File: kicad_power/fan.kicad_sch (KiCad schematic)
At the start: 5 parts, among them M1 Fan, Q5 2N7002E, U7 SFH617A-1X007T

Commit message: finished initial layout of power stage in KiCAD
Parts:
- M1: now left out of the parts list
- Q5: Partno (none) -> 2N7002E-T1-GE3
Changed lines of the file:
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@@
 			)
 		)
-		(property "Description" "Resistor"
+		(property "Description" "125mW Thin Film Resistor ±25ppm/℃ ±0.1% 2kΩ 0603 Chip Resistor - Surface Mount ROHS"
 			(at 152.4 92.71 0)
 			(effects
@@
 		(unit 1)
 		(exclude_from_sim no)
-		(in_bom yes)
+		(in_bom no)
 		(on_board yes)
 		(dnp no)
@@
 			)
 		)
-		(property "Description" "Resistor"
+		(property "Description" "Res Thick Film 0603 430 Ohm 1% 0.25W(1/4W) ±100ppm/C Pad SMD T/R Automotive AEC-Q200"
 			(at 118.11 101.6 0)
 			(effects
@@
 			(at 165.1 85.09 0)
 			(effects
+				(font
+					(size 1.27 1.27)
+				)
+				(hide yes)
+			)
+		)
+		(property "Partno" "2N7002E-T1-GE3"
+			(at 165.1 85.09 0)
+			(effects
+				(font
+					(size 1.27 1.27)
+				)
+				(hide yes)
+			)
+		)
+		(property "Field6" ""
+			(at 165.1 85.09 0)
+			(effects

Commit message: adjustment to PCB layout, created BOM file, added MOSFET gate discharge diodes
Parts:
- M1: now in the parts list
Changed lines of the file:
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@@
 		(unit 1)
 		(exclude_from_sim no)
-		(in_bom no)
+		(in_bom yes)
 		(on_board yes)
 		(dnp no)

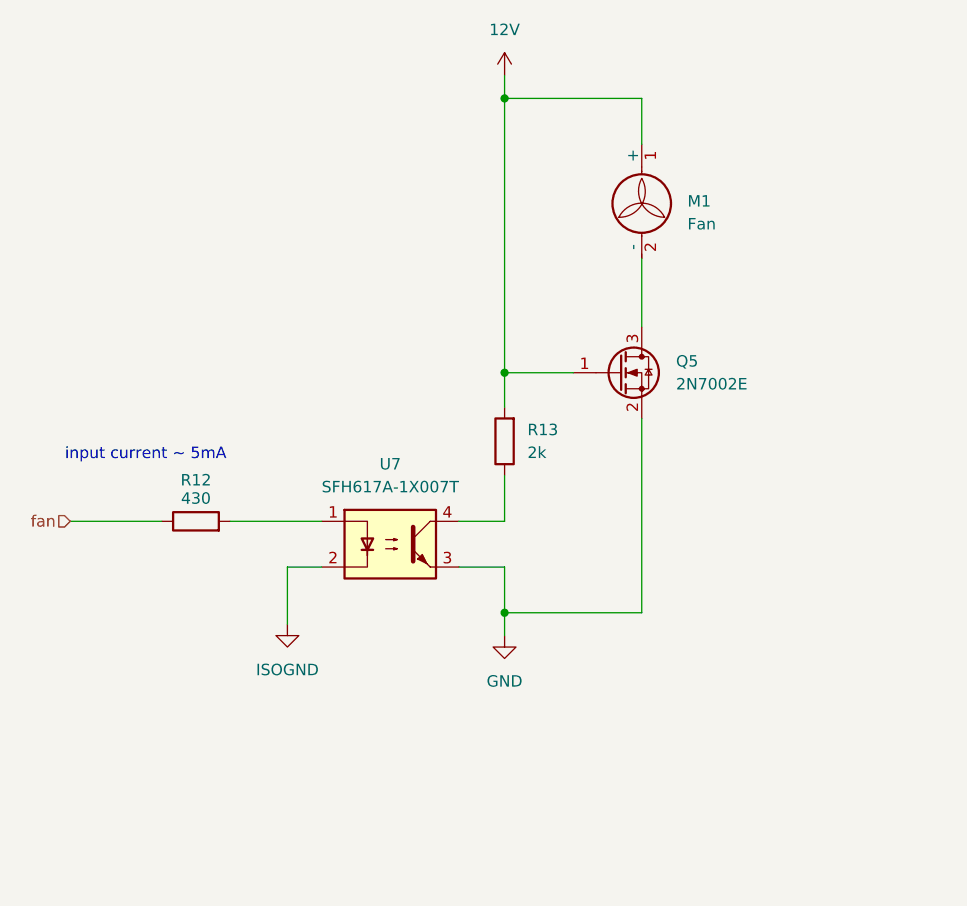
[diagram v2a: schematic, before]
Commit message: introduced AGND and A3V3, ensures HV design rules
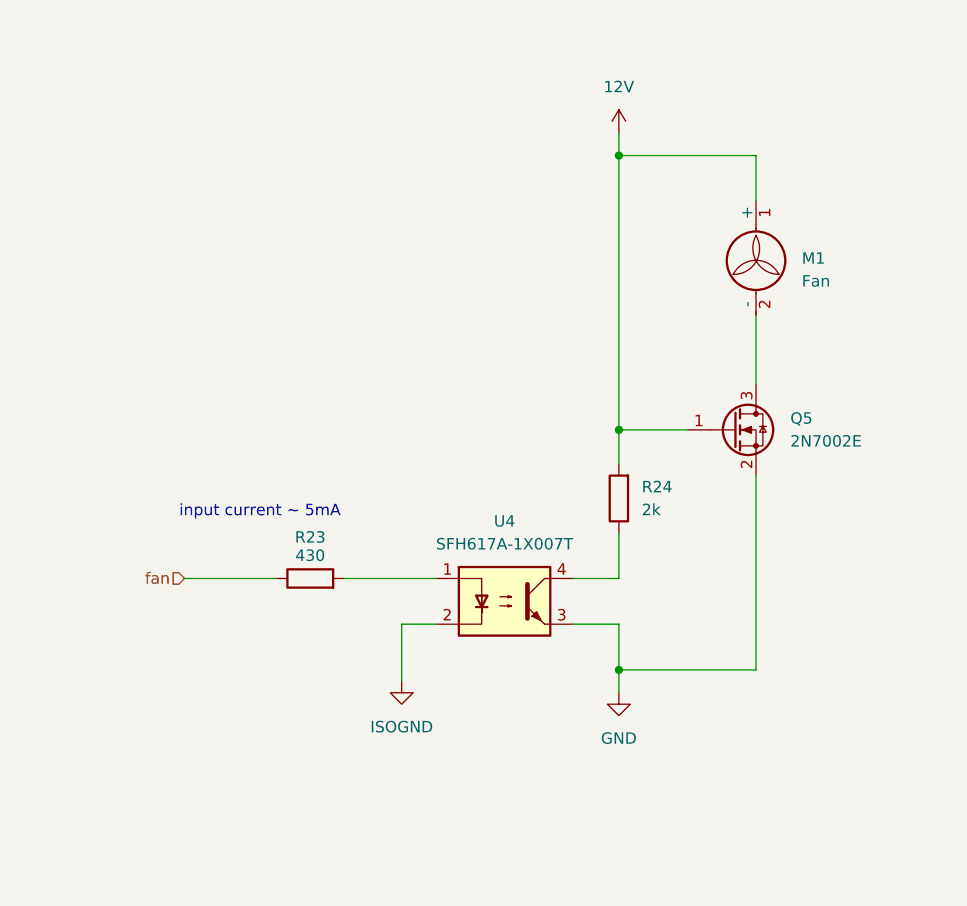
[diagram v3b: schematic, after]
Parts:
- M1: now left out of the parts list
- renumbered R12 to R23, R13 to R24, U7 to U4
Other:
- title: (none) -> Cooling Fan Control
- moved on the sheet: M1, Q5, R23, R24, U4

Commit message: finished initial version of power PCB
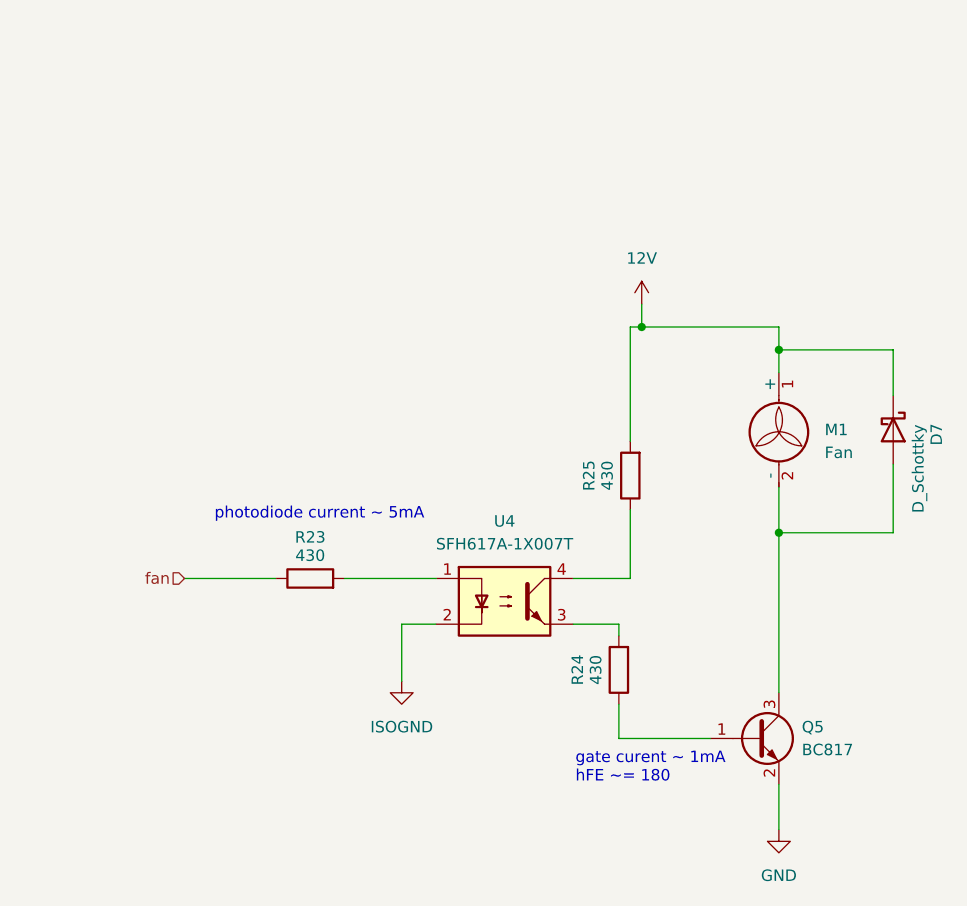
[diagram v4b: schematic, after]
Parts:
- removed Q5: 2N7002E, Package_TO_SOT_SMD:SOT-23, symbol Transistor_FET:2N7002E
- added D7: D_Schottky, Diode_SMD:D_SOD-323F, symbol Device:D_Schottky
- added Q5: BC817, Package_TO_SOT_SMD:SOT-23, symbol Transistor_BJT:BC817
- added R25: 430, Resistor_SMD:R_0603_1608Metric, symbol Device:R
- R24: value 2k -> 430; Partno TNPW06032K00BEEA -> ERJ-PA3F4300V
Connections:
- net 12V: now also D7.1 (K), R25.2; no longer R24.2
- net GND: now also Q5.2 (E); no longer U4.3
- net at R24.1: now also Q5.1 (B); no longer U4.4
- net at M1.2 (-): now also D7.2 (A), Q5.3 (C)
- new net: R24.2, U4.3
- new net: R25.1, U4.4
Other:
- note added: "gate curent ~ 1mA hFE ~= 180"
- note added: "photodiode current ~ 5mA"
- note removed: "input current ~ 5mA"
- moved on the sheet: M1

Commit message: finished version 1.1 of power board
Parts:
- added C34: 2.2u, Capacitor_SMD:C_0603_1608Metric, symbol Device:C
- D7: JLCPCB (none) -> C124210
- M1: JLCPCB (none) -> -; Partno (none) -> -
- Q5: JLCPCB (none) -> C2137
- R23, R24, R25: JLCPCB (none) -> C23170
- U4: JLCPCB (none) -> -
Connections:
- net 12V: now also C34.1
- net at D7.2 (A), M1.2 (-), Q5.3 (C): now also C34.2
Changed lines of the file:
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@@
 		(title "Cooling Fan Control")
 		(date "2025-08-07")
+		(rev "1.1")
 	)
 	(text "gate curent ~ 1mA\nhFE ~= 180"
@@
 	(wire
 		(pts
+			(xy 173.99 82.55) (xy 182.88 82.55)
+		)
+		(stroke
+			(width 0)
+			(type default)
+		)
+	)
+	(wire
+		(pts
+			(xy 173.99 102.87) (xy 182.88 102.87)
+		)
+		(stroke
+			(width 0)
+			(type default)
+		)
+	)
+	(wire
+		(pts
 			(xy 166.37 80.01) (xy 167.64 80.01)
 		)
@@
 	(wire
 		(pts
+			(xy 173.99 95.25) (xy 173.99 102.87)
+		)
+		(stroke
+			(width 0)
+			(type default)
+		)
+	)
+	(wire
+		(pts
 			(xy 182.88 97.79) (xy 182.88 102.87)
 		)
@@
 		(pts
 			(xy 144.78 113.03) (xy 140.97 113.03)
+		)
+		(stroke
+			(width 0)
+			(type default)
+		)
+	)
+	(wire
+		(pts
+			(xy 173.99 87.63) (xy 173.99 82.55)
 		)
 		(stroke
@@
 			)
 		)
+		(property "JLCPCB" "C23170"
+			(at 165.1 118.11 90)
+			(effects
+				(font
+					(size 1.27 1.27)
+				)
+				(hide yes)
+			)
+		)
 		(pin "1"
 		)
@@
 			)
 		)
+		(property "JLCPCB" "-"
+			(at 182.88 92.71 0)
+			(effects
+				(font
+					(size 1.27 1.27)
+				)
+				(hide yes)
+			)
+		)
+		(property "Partno" "-"
+			(at 182.88 92.71 0)
+			(effects
+				(font
+					(size 1.27 1.27)
+				)
+				(hide yes)
+			)
+		)
 		(pin "1"
 		)
@@
 		)
 		(property "Partno" "ERJ-PA3F4300V"
+			(at 130.81 107.95 90)
+			(effects
+				(font
+					(size 1.27 1.27)
+				)
+				(hide yes)
+			)
+		)
+		(property "JLCPCB" "C23170"
 			(at 130.81 107.95 90)
 			(effects
@@
 			)
 		)
+		(property "JLCPCB" "-"
+			(at 152.4 110.49 0)
+			(effects
+				(font
+					(size 1.27 1.27)
+				)
+				(hide yes)
+			)
+		)
 		(pin "1"
 		)
@@
 			)
 		)
+		(property "JLCPCB" "C124210"
+			(at 195.58 91.44 0)
+			(effects
+				(font
+					(size 1.27 1.27)
+				)
+				(hide yes)
+			)
+		)
 		(pin "1"
 		)
@@
 				(path "/b0a218b5-3684-447f-8dec-1dd61a8887f1/92cb4394-a405-4920-b688-0d74a92f3960"
 					(reference "D7")
+					(unit 1)
+				)
+			)
+		)
+	)
+	(symbol
+		(lib_id "Device:C")
+		(at 173.99 91.44 0)
+		(unit 1)
+		(exclude_from_sim no)
+		(in_bom yes)
+		(on_board yes)
+		(dnp no)
+		(property "Reference" "C34"
+			(at 169.672 89.154 0)
+			(effects
+				(font
+					(size 1.27 1.27)
+				)
+				(justify left)
+			)
+		)
+		(property "Value" "2.2u"
+			(at 174.498 93.726 0)
+			(effects
+				(font
+					(size 1.27 1.27)
+				)
+				(justify left)
+			)
+		)
+		(property "Footprint" "Capacitor_SMD:C_0603_1608Metric"
+			(at 174.9552 95.25 0)
+			(effects
+				(font
+					(size 1.27 1.27)
+				)
+				(hide yes)
+			)
+		)
+		(property "Datasheet" "https://octopart.com/datasheet/cga3e1x7s1c225k080ae-tdk-68305583"
+			(at 173.99 91.44 0)
+			(effects
+				(font
+					(size 1.27 1.27)
+				)
+				(hide yes)
+			)
+		)
+		(property "Description" "Cap Ceramic 2.2uF 16V X7S 10% Pad SMD 0603 Soft Termination 125C Automotive T/R"
+			(at 173.99 91.44 0)
+			(effects
+				(font
+					(size 1.27 1.27)
+				)
+				(hide yes)
+			)
+		)
+		(property "Partno" "CGA3E1X7S1C225K080AE"
+			(at 173.99 91.44 0)
+			(effects
+				(font
+					(size 1.27 1.27)
+				)
+				(hide yes)
+			)
+		)
+		(property "JLCPCB" "CL10A225KA8NNNC"
+			(at 173.99 91.44 0)
+			(effects
+				(font
+					(size 1.27 1.27)
+				)
+				(hide yes)
+			)
+		)
+		(pin "1"
+		)
+		(pin "2"
+		)
+		(instances
+			(project "mdriver_hw_power"
+				(path "/b0a218b5-3684-447f-8dec-1dd61a8887f1/92cb4394-a405-4920-b688-0d74a92f3960"
+					(reference "C34")
 					(unit 1)
 				)
@@
 			)
 		)
+		(property "JLCPCB" "C23170"
+			(at 166.37 96.52 90)
+			(effects
+				(font
+					(size 1.27 1.27)
+				)
+				(hide yes)
+			)
+		)
 		(pin "1"
 		)
@@
 			(at 180.34 125.73 0)
 			(effects
+				(font
+					(size 1.27 1.27)
+				)
+				(hide yes)
+			)
+		)
+		(property "JLCPCB" "C2137"
+			(at 180.34 125.73 0)
+			(effects
